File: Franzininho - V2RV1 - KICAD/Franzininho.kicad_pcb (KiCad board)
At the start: 2 copper layers, 51.1 x 30 mm, 30 parts, among them IC1 ATTINY85 - 20PU, J1 M03PTH, U1 L78L05_TO92, X1 USB-A-H

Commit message: V2RV2 - Corrigido GND no C2
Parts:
- renumbered LED to LED1, ON to ON1, RESET to RESET1
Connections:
- C2 pad 1: (no net) -> 5V
- C2 pad 2: (no net) -> GND
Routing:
- net 5V: track 135.9 -> 141.5 mm
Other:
- board text added: "V2RV2"
- board text removed: "V2RV1"
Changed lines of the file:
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@@
-(kicad_pcb (version 20171130) (host pcbnew "(5.0.0)")
+(kicad_pcb (version 20171130) (host pcbnew 5.1.4-e60b266~84~ubuntu18.04.1)
   (general
     (thickness 1.6)
     (drawings 26)
-    (tracks 153)
+    (tracks 157)
     (zones 0)
     (modules 30)
@@
   )
   (setup
-    (last_trace_width 0.25)
+    (last_trace_width 0.508)
     (user_trace_width 0.1524)
     (user_trace_width 0.254)
@@
     (zone_45_only no)
     (trace_min 0.1524)
-    (segment_width 0.2)
-    (edge_width 0.15)
     (via_size 0.8)
     (via_drill 0.4)
@@
     (uvia_min_size 0.2)
     (uvia_min_drill 0.1)
+    (edge_width 0.15)
+    (segment_width 0.2)
     (pcb_text_width 0.3)
     (pcb_text_size 1.5 1.5)
@@
     (at 144.272 116.078 90)
     (descr "<B>LED</B><p>\n3 mm, round")
-    (fp_text reference ON (at 3.81 1.143) (layer F.SilkS)
+    (fp_text reference ON1 (at 3.81 1.143) (layer F.SilkS)
       (effects (font (size 1.2 1.2) (thickness 0.1524)) (justify right top))
     )
@@
     (at 149.352 116.078 90)
     (descr "<B>LED</B><p>\n3 mm, round")
-    (fp_text reference LED (at 3.81 1.524) (layer F.SilkS)
+    (fp_text reference LED1 (at 3.81 1.524) (layer F.SilkS)
       (effects (font (size 1.2 1.2) (thickness 0.1524)) (justify right top))
     )
@@
   (module Franzininho:TAC-SWITCH-PTH locked (layer Top)
     (at 160.528 94.234 180)
-    (fp_text reference RESET (at -5.3848 3.302 90) (layer F.SilkS)
+    (fp_text reference RESET1 (at -5.3848 3.302 90) (layer F.SilkS)
       (effects (font (size 1.2065 1.2065) (thickness 0.1524)) (justify right top))
     )
@@
     (fp_arc (start 1.25 0) (end -1.05558 1.18) (angle -125.8) (layer F.SilkS) (width 0.12))
     (fp_arc (start 1.25 0) (end -1.05558 -1.18) (angle 125.8) (layer F.SilkS) (width 0.12))
-    (pad 2 thru_hole circle (at 2.5 0 270) (size 1.6 1.6) (drill 0.8) (layers *.Cu *.Mask))
-    (pad 1 thru_hole rect (at 0 0 270) (size 1.6 1.6) (drill 0.8) (layers *.Cu *.Mask))
+    (pad 2 thru_hole circle (at 2.5 0 270) (size 1.6 1.6) (drill 0.8) (layers *.Cu *.Mask)
+      (net 1 GND))
+    (pad 1 thru_hole rect (at 0 0 270) (size 1.6 1.6) (drill 0.8) (layers *.Cu *.Mask)
+      (net 2 5V))
     (model ${KISYS3DMOD}/Capacitors_THT.3dshapes/CP_Radial_D5.0mm_P2.50mm.wrl
       (at (xyz 0 0 0))
@@
     (effects (font (size 1.2 1.2) (thickness 0.1524)) (justify right top))
   )
-  (gr_text V2RV1 (at 124.333 118.11) (layer F.SilkS)
+  (gr_text V2RV2 (at 124.333 118.11) (layer F.SilkS)
     (effects (font (size 1 1) (thickness 0.1524)) (justify left bottom))
   )
@@
   (segment (start 148.89235 91.9761) (end 151.11485 91.9761) (width 0.8128) (layer Bottom) (net 2))
   (segment (start 151.11485 91.9761) (end 151.74985 92.6111) (width 0.8128) (layer Bottom) (net 2))
-  (segment (start 151.74985 92.6111) (end 151.74985 97.15135) (width 0.8128) (layer Bottom) (net 2))
   (segment (start 148.89235 91.9761) (end 148.89235 93.2461) (width 0.8128) (layer Bottom) (net 2))
   (segment (start 148.89235 93.2461) (end 146.98735 95.1511) (width 0.8128) (layer Bottom) (net 2))
@@
   (segment (start 164.084 108.312) (end 161.436 105.664) (width 0.508) (layer Bottom) (net 2))
   (segment (start 164.084 108.712) (end 164.084 108.312) (width 0.508) (layer Bottom) (net 2))
-  (segment (start 154.330621 94.570579) (end 152.638849 96.262351) (width 0.508) (layer Bottom) (net 2))
-  (segment (start 152.638849 96.262351) (end 151.74985 97.15135) (width 0.508) (layer Bottom) (net 2))
   (segment (start 160.996733 94.287989) (end 160.714143 94.570579) (width 0.508) (layer Bottom) (net 2))
   (segment (start 165.901267 94.287989) (end 160.996733 94.287989) (width 0.508) (layer Bottom) (net 2))
@@
   (segment (start 171.43485 99.29885) (end 171.43485 113.5661) (width 0.508) (layer Bottom) (net 2))
   (segment (start 170.6571 98.5211) (end 171.43485 99.29885) (width 0.508) (layer Bottom) (net 2))
+  (segment (start 151.74985 92.6111) (end 151.74985 97.15135) (width 0.8128) (layer Bottom) (net 2))
+  (segment (start 151.892 92.75325) (end 151.74985 92.6111) (width 0.8128) (layer Bottom) (net 2))
+  (segment (start 151.892 97.282) (end 151.892 92.75325) (width 0.8128) (layer Bottom) (net 2))
+  (segment (start 151.892 97.282) (end 153.2 97.282) (width 0.508) (layer Bottom) (net 2))
+  (segment (start 153.7006 96.7814) (end 153.7006 95.2006) (width 0.508) (layer Bottom) (net 2))
+  (segment (start 153.2 97.282) (end 153.7006 96.7814) (width 0.508) (layer Bottom) (net 2))
+  (segment (start 154.330621 94.570579) (end 153.7006 95.2006) (width 0.508) (layer Bottom) (net 2))
   (segment (start 137.16 100.934973) (end 133.835527 97.6105) (width 0.508) (layer Bottom) (net 3))
   (segment (start 137.16 113.538) (end 137.16 100.934973) (width 0.508) (layer Bottom) (net 3))

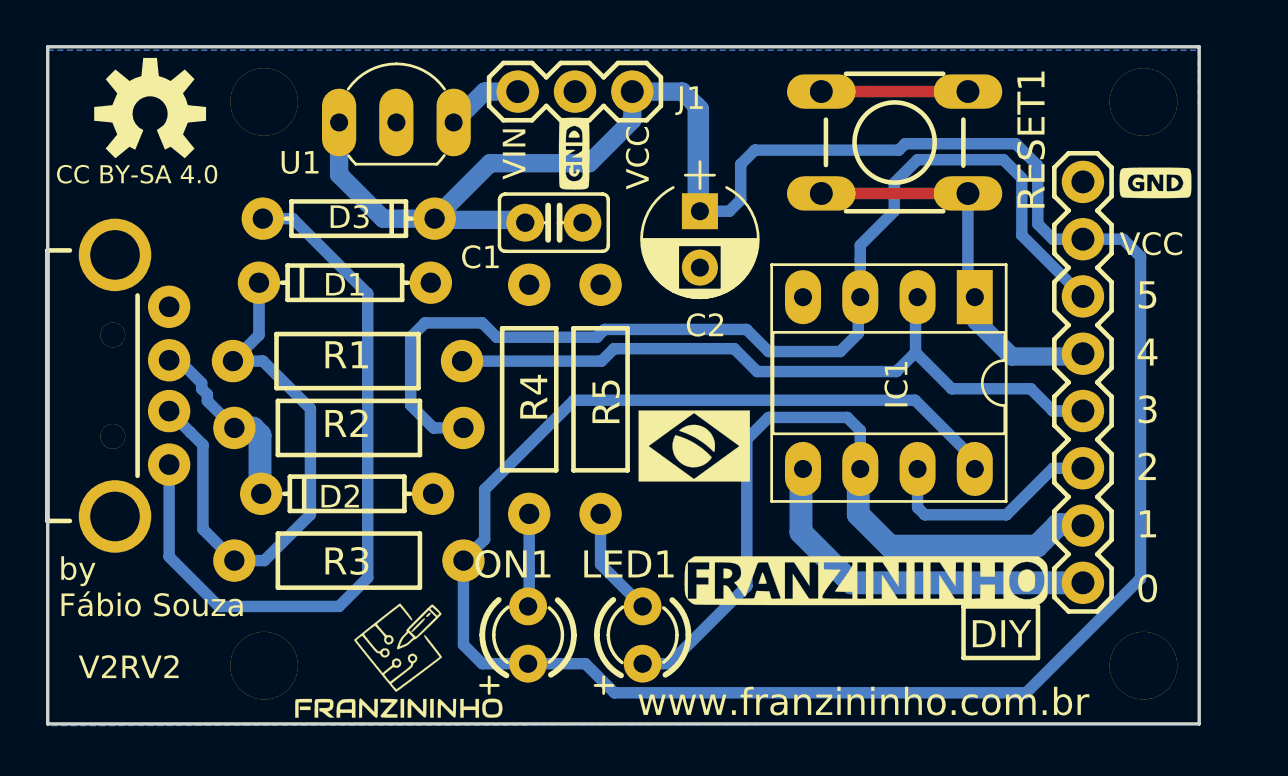
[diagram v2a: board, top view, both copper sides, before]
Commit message: Improved production time
Improved copper filled zones
Improved some tracks
Migrated to last version of KiCad
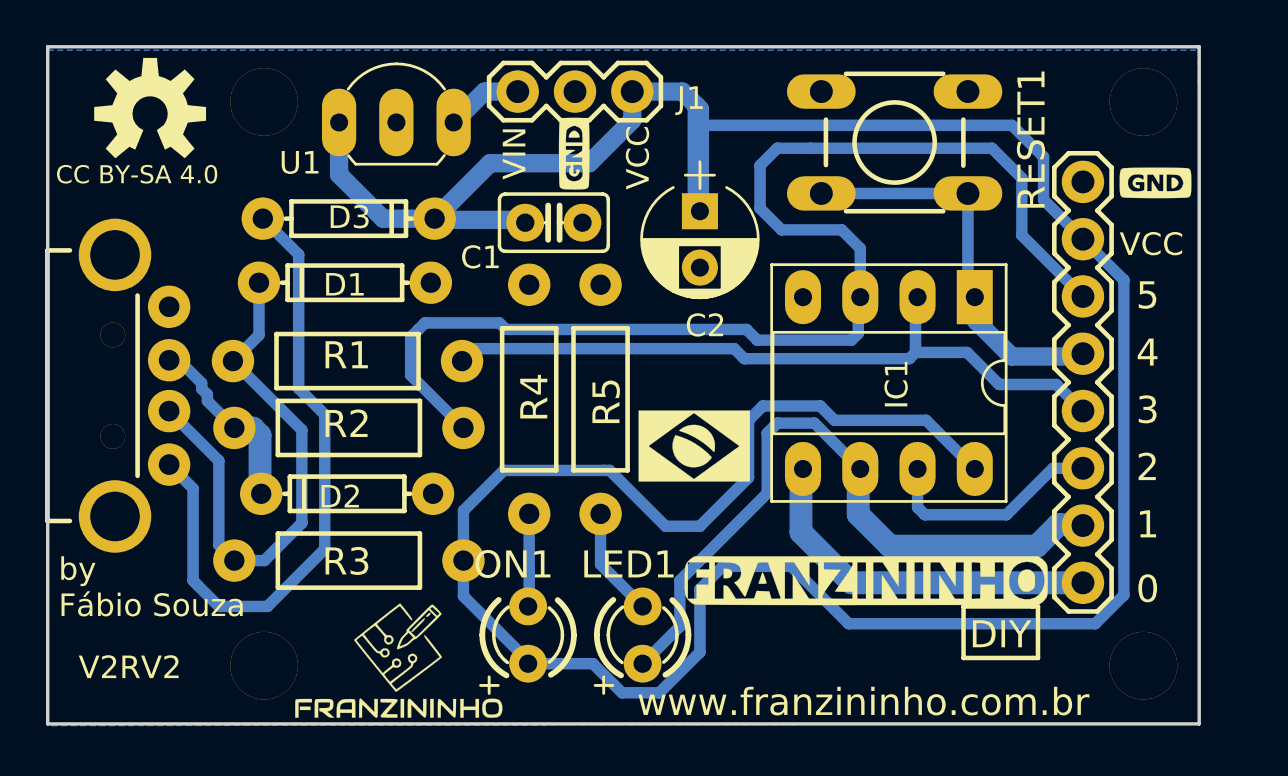
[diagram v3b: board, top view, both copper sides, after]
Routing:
- net Net-(IC1-Pad3): track 47.7 -> 55.8 mm
- net GND: track 6.50 -> 0.00 mm
- net 5V: track 141.5 -> 147.1 mm
- net Net-(D3-PadA): track 33.0 -> 28.7 mm
- net Net-(IC1-Pad6): track 32.8 -> 30.6 mm
- net Net-(D1-PadC): track 25.0 -> 23.9 mm
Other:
- net class Default removed
